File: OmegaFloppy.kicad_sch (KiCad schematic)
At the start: 18 parts, among them J1 DIN-6, J2 USB_C_Receptacle_USB2.0_16P, J3 AVR-ISP-6, U1 ATmega32U2-M, U2 74LS06, U3 TPD2EUSB30, Y1 16 MHz

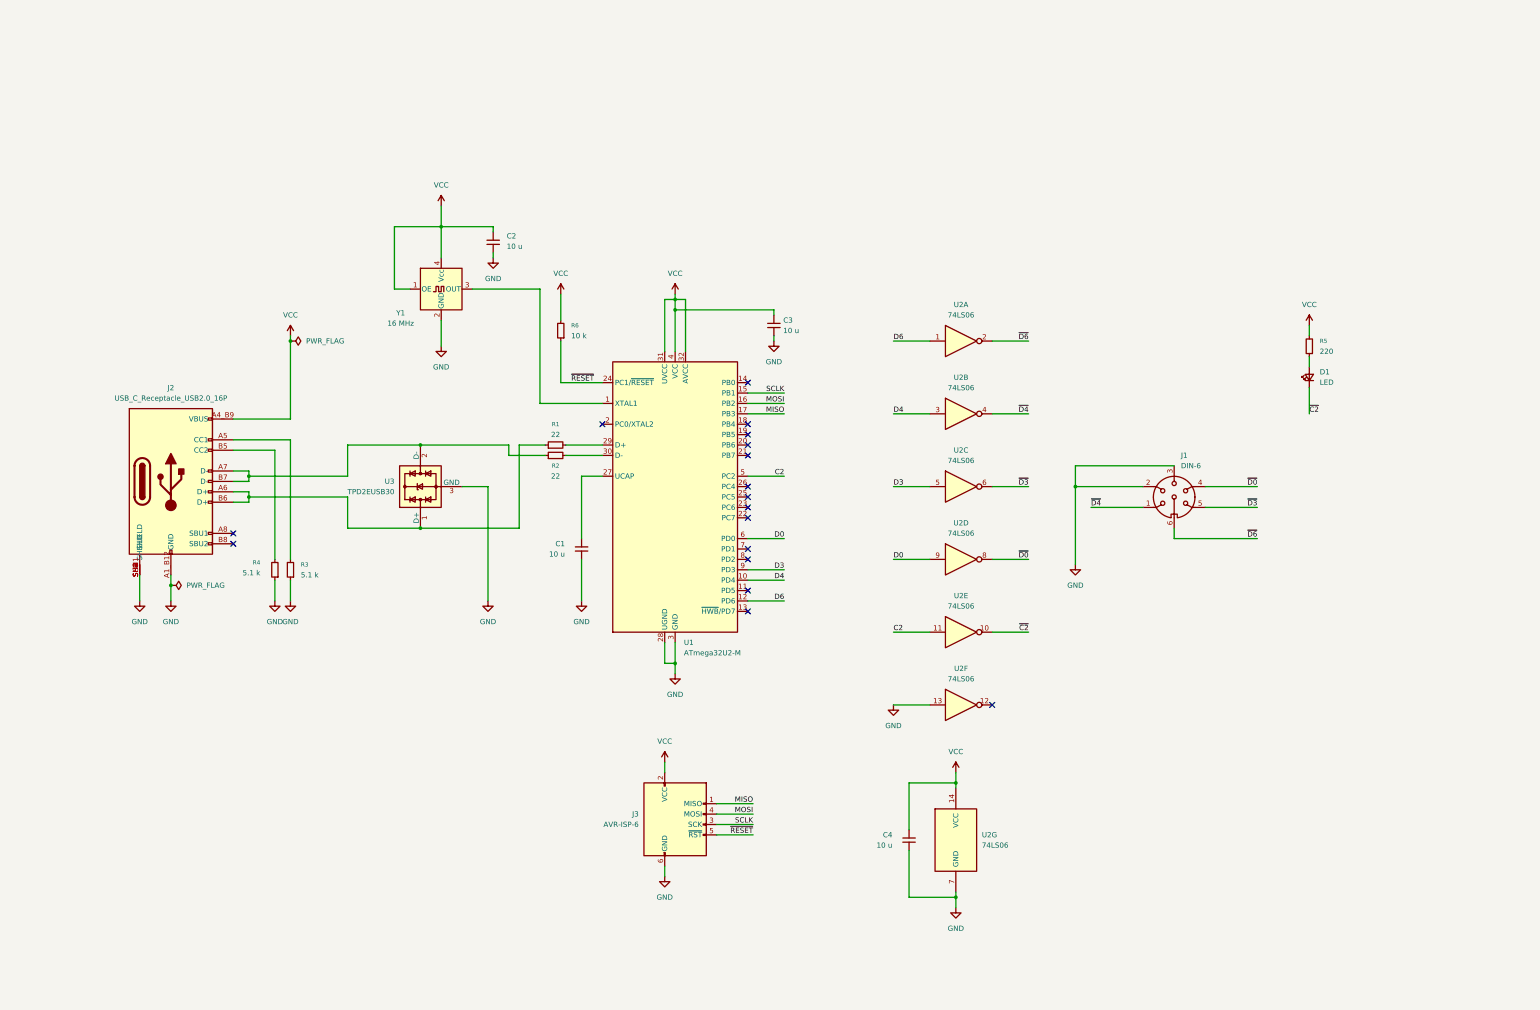
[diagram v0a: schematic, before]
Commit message: fixed missing connection on IEC port
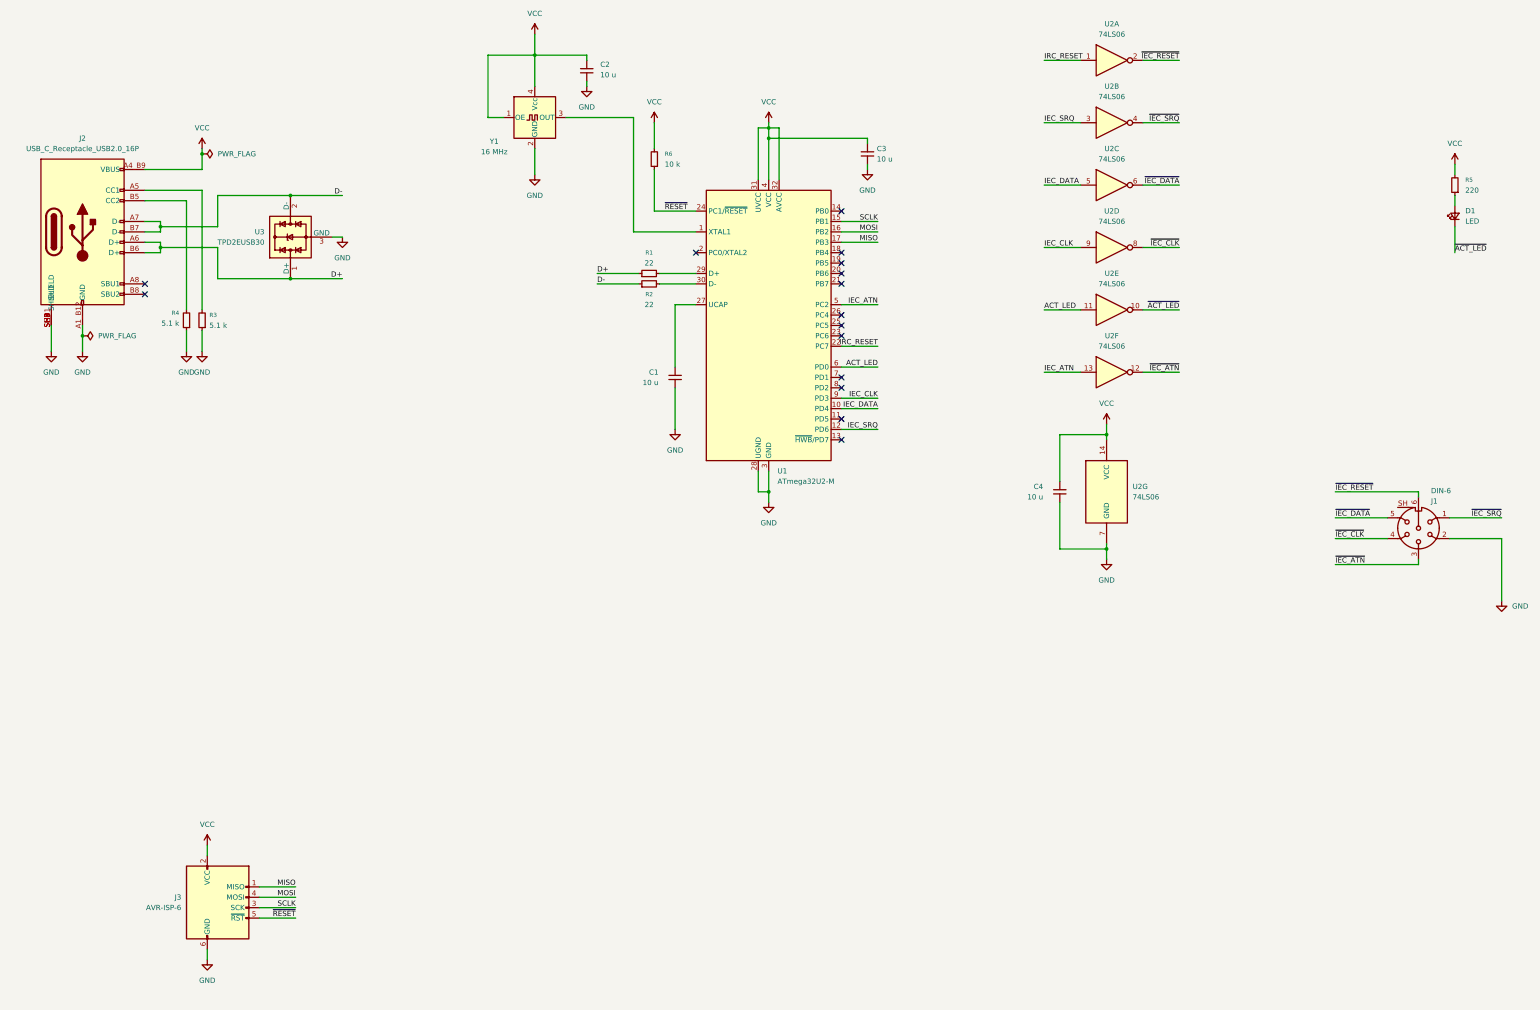
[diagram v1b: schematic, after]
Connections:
- net GND: no longer J1.3, U2.13
- net ~{IEC_ATN}: now reaches U2.12
- net ~{IEC_ATN}: now also J1.3
- net IRC_RESET: now reaches U1.22 (PC7)
- net IRC_RESET: now also U2.1
- net D+: now reaches J2.A6 (D+), J2.B6 (D+), R1.1, U3.1 (D+)
- net D-: now reaches J2.A7 (D-), J2.B7 (D-), R2.1, U3.2 (D-)
- net C2 renamed ACT_LED
- net ACT_LED: now also U1.6 (PD0); no longer U1.5 (PC2)
- net D0 renamed IEC_CLK
- net IEC_CLK: now also U1.9 (PD3); no longer U1.6 (PD0)
- net D3 renamed IEC_DATA
- net IEC_DATA: now also U1.10 (PD4); no longer U1.9 (PD3)
- net D4 renamed IEC_SRQ
- net IEC_SRQ: now also U1.12 (PD6); no longer U1.10 (PD4)
- removed net D6: U1.12 (PD6), U2.1
- net ~{C2} renamed ~{ACT_LED}
- net ~{D0} renamed ~{IEC_CLK}
- net ~{D3} renamed ~{IEC_DATA}
- net ~{D4} renamed ~{IEC_SRQ}
- net ~{D6} renamed ~{IEC_RESET}
- new net IEC_ATN: U1.5 (PC2), U2.13
- no-connect marks 17 -> 15
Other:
- moved on the sheet: C1, C2, C3, C4, D1, J2, J3, R1, R2, R3, R4, R5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

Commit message: cleaned up the schematics
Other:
- note added: "IEC Connection"
- note added: "ISP Programming Pads"
- note added: "LED Indicator"
- note added: "Microcontroller"
- note added: "Schmidt Triggers/ Inverters"
- note added: "USB Connection"
- moved on the sheet: C1, C2, C3, C4, D1, J1, J2, J3, R1, R2, R3, R4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

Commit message: added missing input pins
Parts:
- added D2: Power (green), LED_SMD:LED_0402_1005Metric, symbol Device:LED_Small
- added R10, R11, R7, R8, R9: 100 k, Resistor_SMD:R_0402_1005Metric, symbol Device:R_Small
- added R12: 220, Resistor_SMD:R_0402_1005Metric, symbol Device:R_Small
- D1: value LED -> Activity (red); MPN IN-S42DS5G -> IN-S42DS5R
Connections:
- net IEC_ATN is gone; now on net ACT_LED: U1.5 (PC2), U2.13
- net ACT_LED: no longer U1.6 (PD0), U2.11
- net GND: now also D2.1 (K)
- net VCC: now also R12.2
- net ~{ACT_LED}: now also U2.12; no longer U2.10
- net IO_SRQ_IN: now reaches U1.11 (PD5)
- net IO_SRQ_IN: now also R9.2
- net IO_RESET_IN: now reaches U1.13 (~{HWB}/PD7)
- net IO_RESET_IN: now also R8.2
- net IO_ATN_IN: now reaches U1.23 (PC6)
- net IO_ATN_IN: now also R7.2
- net IO_CLK_IN: now reaches U1.7 (PD1)
- net IO_CLK_IN: now also R11.2
- net IO_DATA_IN: now reaches U1.8 (PD2)
- net IO_DATA_IN: now also R10.2
- net IEC_CLK renamed IO_DATA
- net IEC_DATA renamed IO_SRQ
- net IEC_SRQ renamed IO_RESET
- net IRC_RESET renamed IO_ATN
- net ~{IEC_ATN} renamed ~{IO_ATN}
- net ~{IO_ATN}: now also U2.2, R7.1; no longer U2.12
- net ~{IEC_CLK} renamed ~{IO_CLK}
- net ~{IO_CLK}: now also U2.10, R11.1; no longer U2.8
- net ~{IEC_DATA} renamed ~{IO_DATA}
- net ~{IO_DATA}: now also U2.8, R10.1; no longer U2.6
- net ~{IEC_RESET} renamed ~{IO_RESET}
- net ~{IO_RESET}: now also U2.4, R8.1; no longer U2.2
- net ~{IEC_SRQ} renamed ~{IO_SRQ}
- net ~{IO_SRQ}: now also U2.6, R9.1; no longer U2.4
- new net: D2.2 (A), R12.1
- new net IO_CLK: U1.6 (PD0), U2.11
- no-connect marks 15 -> 10
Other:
- note added: "LED Indicators"
- note removed: "LED Indicator"
- moved on the sheet: C4, U2B, U2C, U2D, U2E, U2F, U2G
